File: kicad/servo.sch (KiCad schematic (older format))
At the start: 0 parts

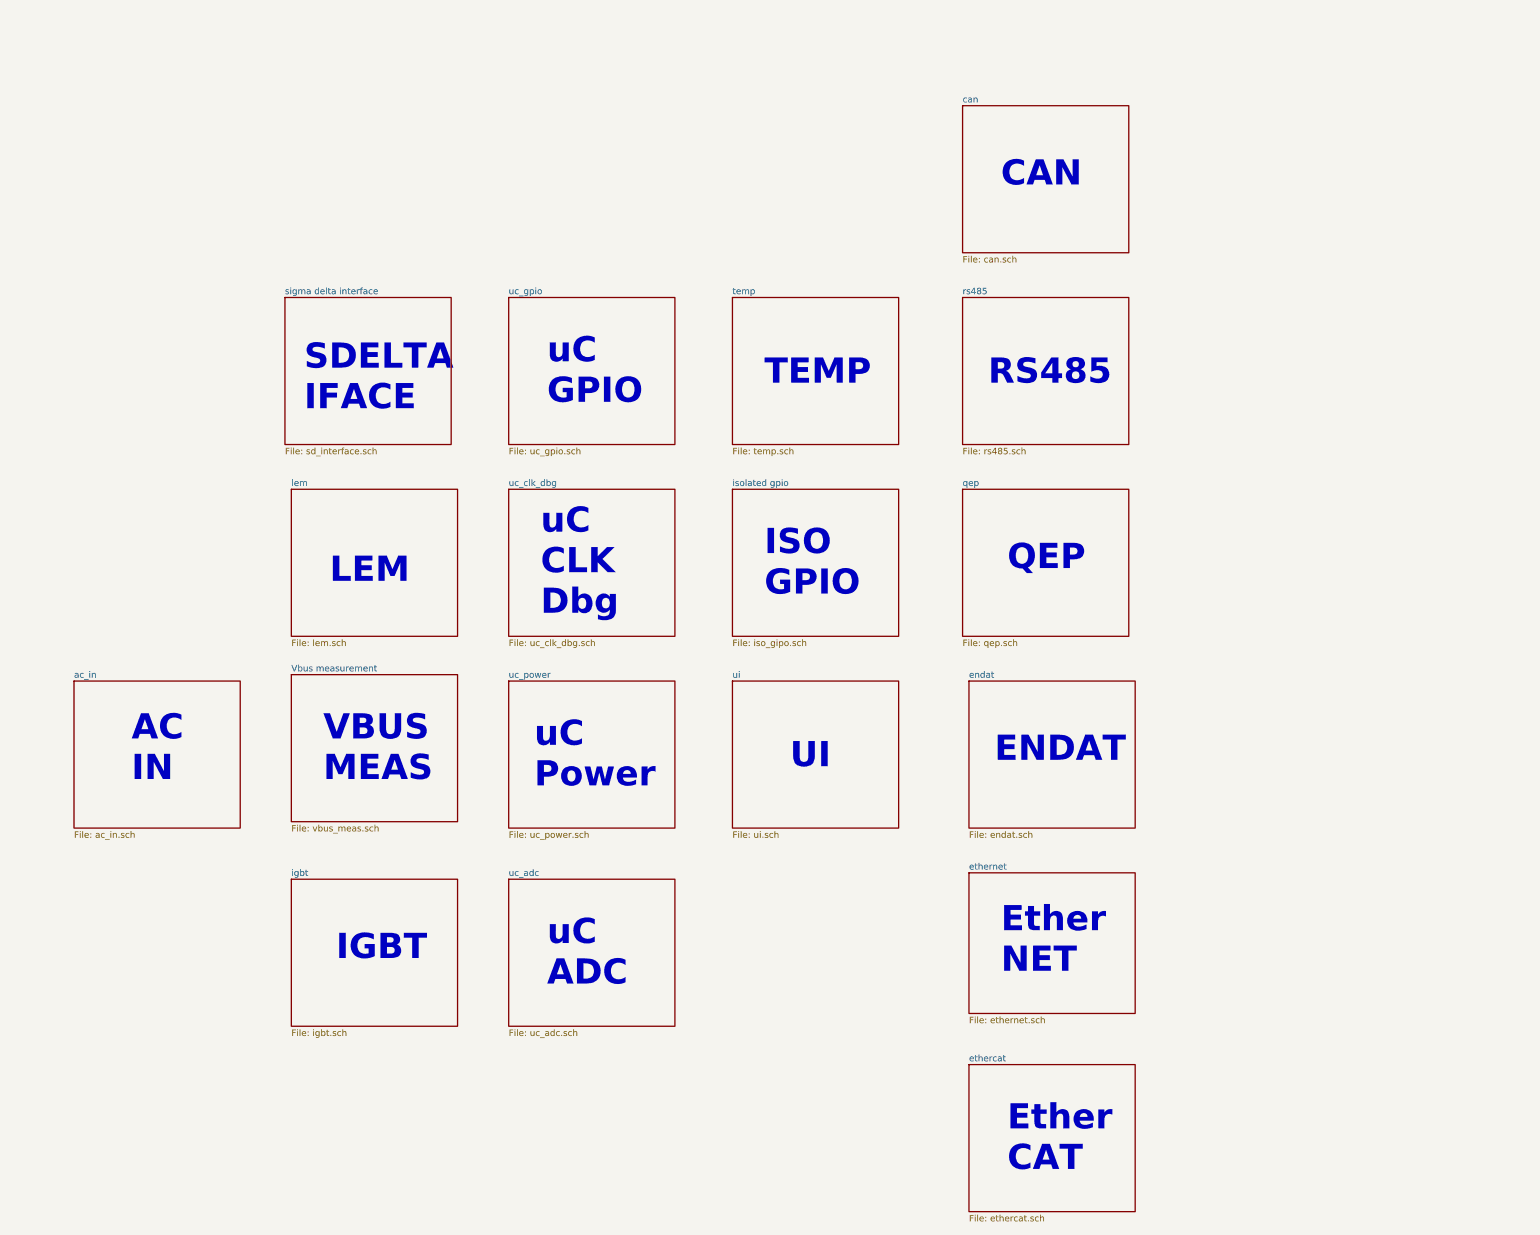
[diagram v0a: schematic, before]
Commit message: remove isolation GPIO's and replace it by free pins at IGBT
I remove completely the isolated inputs pins cause I've 8 pins free at
IGBT isolated interfase, so I leave 4 for outpus and 4 for inputs with
one isolated stage, the same as the previous isolated GPIO sheet..
I've improved the DBG sheet and some other details,. I'm ready to make
some electrical checks and fchoose the parts codes and footprints.. go
for it!
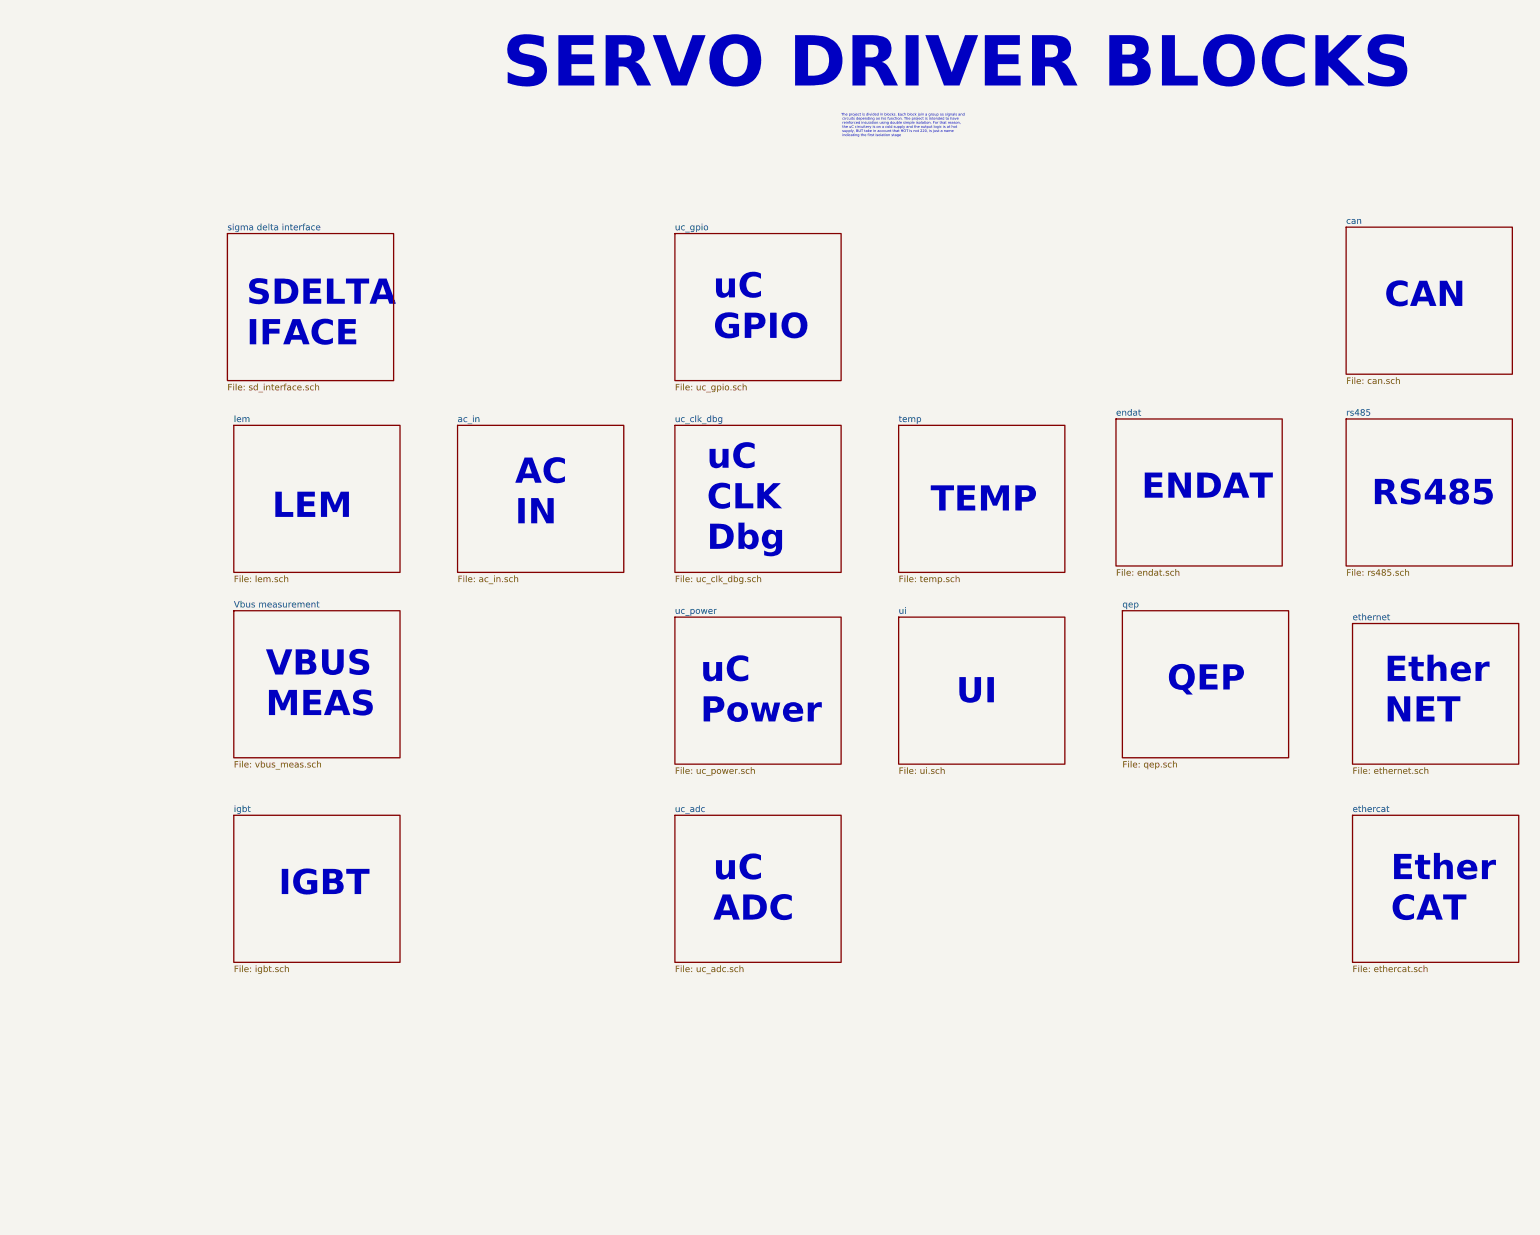
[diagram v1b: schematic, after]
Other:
- note added: "SERVO DRIVER BLOCKS"
- note added: "The project is divided in blocks. Each block join a group os signals and\n circuits depending on his function. The project is intended to have\n reinforced insulation using double simple isolation. For that reason,\n the uC circuitery is on a cold supply and the output logic is at hot\n supply, BUT take in account that HOT is not 220, is just a name\n indicating the first isolation stage\n"
- note removed: "ISO\nGPIO\n"
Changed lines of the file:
@@
 $Descr A3 16535 11693
 encoding utf-8
-Sheet 1 19
+Sheet 1 18
 Title "servo drive"
-Date "25 10 2019"
+Date "2020-01-09"
 Rev "1.0"
 Comp "dci"
@@
 $EndDescr
 $Sheet
-S 9350 7400 1300 1100
+S 12350 5450 1300 1100
 U 5DC3DC9E
 F0 "ethernet" 50
@@
 $EndSheet
 $Sheet
-S 5750 7450 1300 1150
+S 7050 6950 1300 1150
 U 5DD0E9D6
 F0 "uc_adc" 50
@@
 $EndSheet
 $Sheet
-S 9350 8900 1300 1150
+S 12350 6950 1300 1150
 U 5DC4A59D
 F0 "ethercat" 50
@@
 $EndSheet
 $Sheet
-S 5750 5900 1300 1150
+S 7050 5400 1300 1150
 U 5EAA846A
 F0 "uc_power" 50
@@
 $EndSheet
 $Sheet
-S 5750 4400 1300 1150
+S 7050 3900 1300 1150
 U 5DD4DF4C
 F0 "uc_clk_dbg" 50
@@
 $EndSheet
 $Sheet
-S 2350 5900 1300 1150
+S 5350 3900 1300 1150
 U 5DD76B18
 F0 "ac_in" 50
 F1 "ac_in.sch" 50
 $EndSheet
-Text Notes 6050 8300 0    197  ~ 39
+Text Notes 7350 7800 0    197  ~ 39
 uC\nADC
 $Sheet
-S 4050 7450 1300 1150
+S 3600 6950 1300 1150
 U 5DDE8C5E
 F0 "igbt" 50
 F1 "igbt.sch" 50
 $EndSheet
-Text Notes 4400 8100 0    197  ~ 39
+Text Notes 3950 7600 0    197  ~ 39
 IGBT
-Text Notes 5950 6750 0    197  ~ 39
+Text Notes 7250 6250 0    197  ~ 39
 uC \nPower
-Text Notes 9650 9750 0    197  ~ 39
+Text Notes 12650 7800 0    197  ~ 39
 Ether\nCAT
 $Sheet
-S 7500 2900 1300 1150
+S 8800 3900 1300 1150
 U 5DE49152
 F0 "temp" 50
 F1 "temp.sch" 50
 $EndSheet
-Text Notes 7750 3600 0    197  ~ 39
+Text Notes 9050 4600 0    197  ~ 39
 TEMP
-Text Notes 2800 6700 0    197  ~ 39
+Text Notes 5800 4700 0    197  ~ 39
 AC\nIN
-Text Notes 9600 8200 0    197  ~ 39
+Text Notes 12600 6250 0    197  ~ 39
 Ether\nNET
-Text Notes 6000 5400 0    197  ~ 39
+Text Notes 7300 4900 0    197  ~ 39
 uC\nCLK\nDbg
-Text Notes 9550 6550 0    197  ~ 39
+Text Notes 10700 4500 0    197  ~ 39
 ENDAT
 $Sheet
-S 9350 5900 1300 1150
+S 10500 3850 1300 1150
 U 5DE3DF56
 F0 "endat" 50
@@
 $EndSheet
 $Sheet
-S 9300 4400 1300 1150
+S 10550 5350 1300 1150
 U 5E092156
 F0 "qep" 50
 F1 "qep.sch" 50
 $EndSheet
-Text Notes 9650 5050 0    197  ~ 39
+Text Notes 10900 6000 0    197  ~ 39
 QEP
 $Sheet
-S 9300 2900 1300 1150
+S 12300 3850 1300 1150
 U 5E1BAEAA
 F0 "rs485" 50
 F1 "rs485.sch" 50
 $EndSheet
-Text Notes 9500 3600 0    197  ~ 39
+Text Notes 12500 4550 0    197  ~ 39
 RS485
 $Sheet
-S 9300 1400 1300 1150
+S 12300 2350 1300 1150
 U 5E21534F
 F0 "can" 50
 F1 "can.sch" 50
 $EndSheet
-Text Notes 9600 2050 0    197  ~ 39
+Text Notes 12600 3000 0    197  ~ 39
 CAN
 $Sheet
-S 5750 2900 1300 1150
+S 7050 2400 1300 1150
 U 5E033FE4
 F0 "uc_gpio" 50
 F1 "uc_gpio.sch" 50
 $EndSheet
-Text Notes 6050 3750 0    197  ~ 39
+Text Notes 7350 3250 0    197  ~ 39
 uC\nGPIO
 $Sheet
-S 7500 4400 1300 1150
-U 5E0D58C4
-F0 "isolated gpio" 50
-F1 "iso_gipo.sch" 50
-$EndSheet
-Text Notes 7750 5250 0    197  ~ 39
-ISO\nGPIO\n
-$Sheet
-S 7500 5900 1300 1150
+S 8800 5400 1300 1150
 U 5E72D841
 F0 "ui" 50
 F1 "ui.sch" 50
 $EndSheet
-Text Notes 7950 6600 0    197  ~ 39
+Text Notes 9250 6100 0    197  ~ 39
 UI
 $Sheet
-S 4050 4400 1300 1150
+S 3600 3900 1300 1150
 U 605B70F2
 F0 "lem" 50
 F1 "lem.sch" 50
 $EndSheet
-Text Notes 4350 5150 0    197  ~ 39
+Text Notes 3900 4650 0    197  ~ 39
 LEM
 $Sheet
-S 4050 5850 1300 1150
+S 3600 5350 1300 1150
 U 605BEC04
 F0 "Vbus measurement" 50
 F1 "vbus_meas.sch" 50
 $EndSheet
-Text Notes 4300 6700 0    197  ~ 39
+Text Notes 3850 6200 0    197  ~ 39
 VBUS\nMEAS
 $Sheet
-S 4000 2900 1300 1150
+S 3550 2400 1300 1150
 U 5EC40F3C
 F0 "sigma delta interface" 50
 F1 "sd_interface.sch" 50
 $EndSheet
-Text Notes 4150 3800 0    197  ~ 39
+Text Notes 3700 3300 0    197  ~ 39
 SDELTA\nIFACE
+Text Notes 5700 1300 0    394  ~ 79
+SERVO DRIVER BLOCKS
+Text Notes 8350 1650 0    20   ~ 0
+The project is divided in blocks. Each block join a group os signals and\n circuits depending on his function. The project is intended to have\n reinforced insulation using double simple isolation. For that reason,\n the uC circuitery is on a cold supply and the output logic is at hot\n supply, BUT take in account that HOT is not 220, is just a name\n indicating the first isolation stage\n
 $EndSCHEMATC

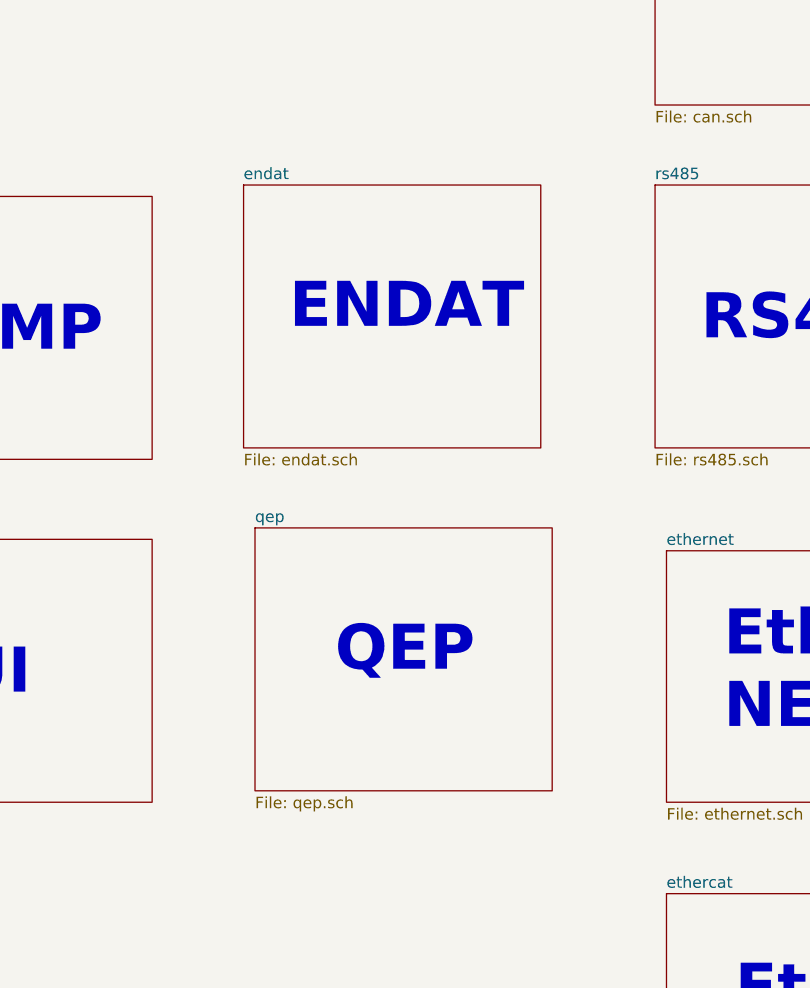
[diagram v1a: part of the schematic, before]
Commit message: added 4 push buttons and more gpios on LCD connector
just to have more UI options. With those I'd manage graphics LCD plus 4
buttons, and charaveter LCD. or the embedded EVE graphic LCD
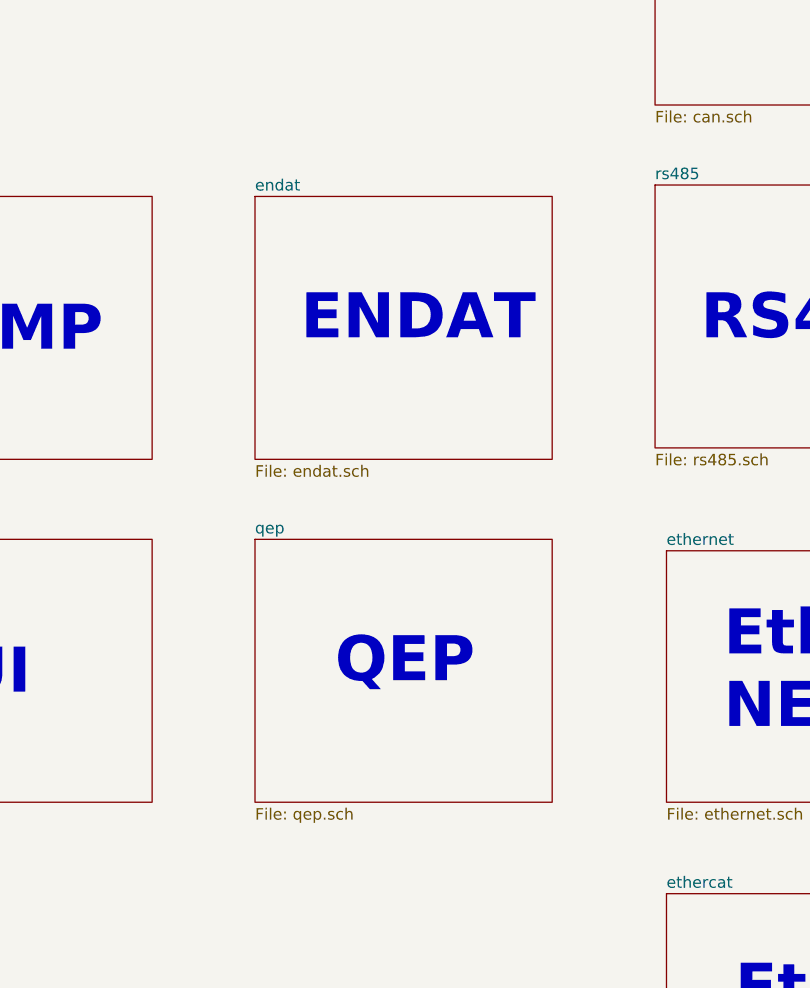
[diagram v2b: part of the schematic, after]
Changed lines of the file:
@@
 Text Notes 7300 4900 0    197  ~ 39
 uC\nCLK\nDbg
-Text Notes 10700 4500 0    197  ~ 39
+Text Notes 10750 4550 0    197  ~ 39
 ENDAT
 $Sheet
-S 10500 3850 1300 1150
+S 10550 3900 1300 1150
 U 5DE3DF56
 F0 "endat" 50
@@
 $EndSheet
 $Sheet
-S 10550 5350 1300 1150
+S 10550 5400 1300 1150
 U 5E092156
 F0 "qep" 50
 F1 "qep.sch" 50
 $EndSheet
-Text Notes 10900 6000 0    197  ~ 39
+Text Notes 10900 6050 0    197  ~ 39
 QEP
 $Sheet

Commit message: I've passed all footprin to layout BUT...
I've passed all, first glance... I need to confirm in details a lot of
things. The objetive for these is to have an aproximation of the size
I'll need to make the board.. then I choose the final detailed footprint
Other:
- note added: "CONN"
- note added: "SDELTA\n"
- note removed: "SDELTA\nIFACE"
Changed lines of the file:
@@
 $Descr A3 16535 11693
 encoding utf-8
-Sheet 1 18
+Sheet 1 19
 Title "servo drive"
 Date "2020-01-09"
@@
 S 3600 5350 1300 1150
 U 605BEC04
-F0 "Vbus measurement" 50
+F0 "Vbus meas" 50
 F1 "vbus_meas.sch" 50
 $EndSheet
@@
 VBUS\nMEAS
 $Sheet
-S 3550 2400 1300 1150
+S 8850 6950 1300 1150
 U 5EC40F3C
-F0 "sigma delta interface" 50
-F1 "sd_interface.sch" 50
+F0 "connectors" 50
+F1 "conn.sch" 50
 $EndSheet
-Text Notes 3700 3300 0    197  ~ 39
-SDELTA\nIFACE
+Text Notes 9100 7650 0    197  ~ 39
+CONN
 Text Notes 5700 1300 0    394  ~ 79
 SERVO DRIVER BLOCKS
 Text Notes 8350 1650 0    20   ~ 0
 The project is divided in blocks. Each block join a group os signals and\n circuits depending on his function. The project is intended to have\n reinforced insulation using double simple isolation. For that reason,\n the uC circuitery is on a cold supply and the output logic is at hot\n supply, BUT take in account that HOT is not 220, is just a name\n indicating the first isolation stage\n
+$Sheet
+S 3600 2350 1300 1150
+U 6056AA11
+F0 "sigma_delta" 50
+F1 "sigma_delta.sch" 50
+$EndSheet
+Text Notes 3700 3050 0    197  ~ 39
+SDELTA\n
 $EndSCHEMATC

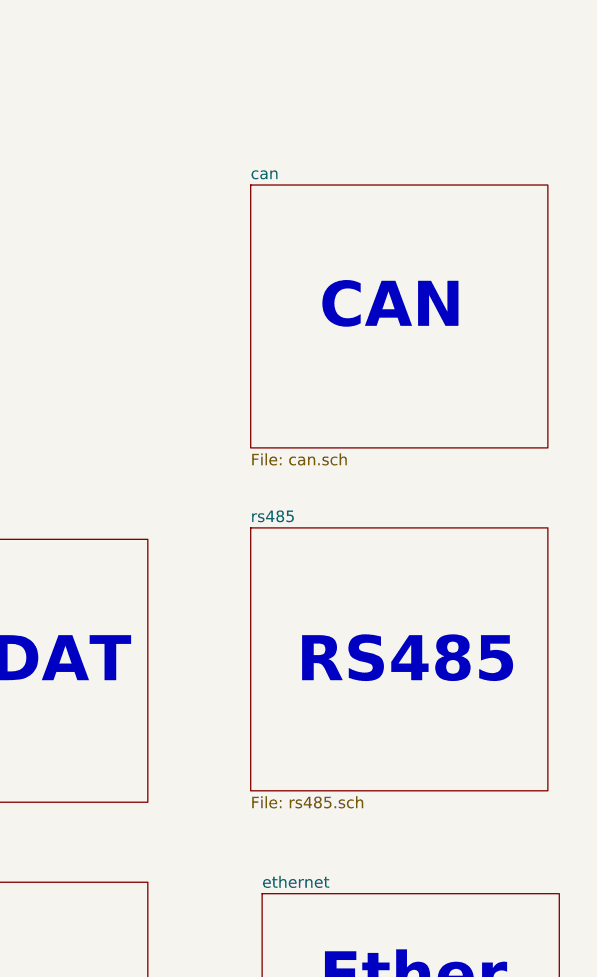
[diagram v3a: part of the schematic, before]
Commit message: changing single row terminal block to double row
I've changed to double row all the connectors, RJ45 and terminal blocks,
I saves spaces and also make it more intuitive related to user
interface..lets go
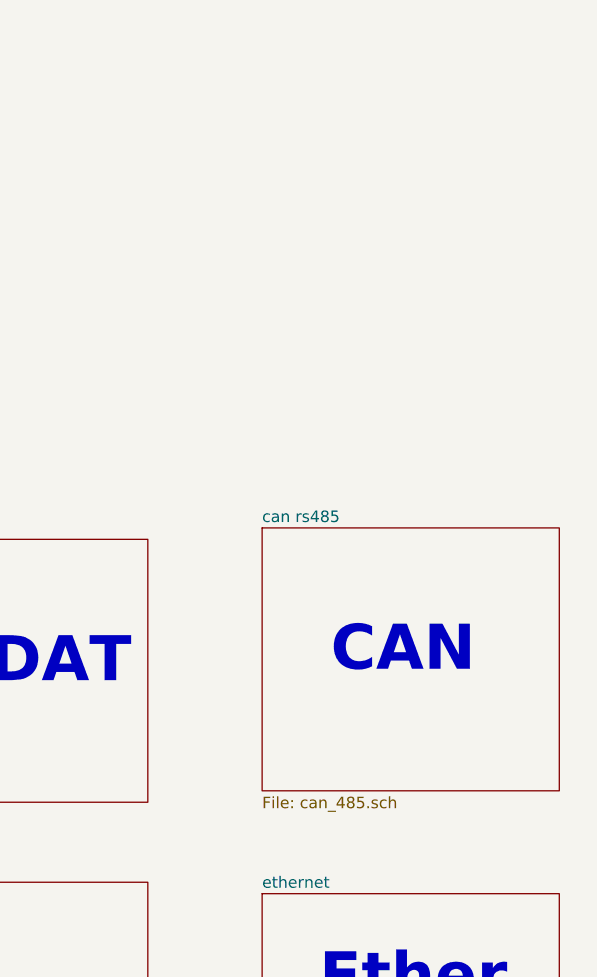
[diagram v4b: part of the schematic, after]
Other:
- note removed: "RS485"
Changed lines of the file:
@@
 $Descr A3 16535 11693
 encoding utf-8
-Sheet 1 19
+Sheet 1 18
 Title "servo drive"
 Date "2020-01-09"
@@
 QEP
 $Sheet
-S 12300 3850 1300 1150
-U 5E1BAEAA
-F0 "rs485" 50
-F1 "rs485.sch" 50
+S 12350 3850 1300 1150
+U 5E21534F
+F0 "can rs485" 50
+F1 "can_485.sch" 50
 $EndSheet
-Text Notes 12500 4550 0    197  ~ 39
-RS485
-$Sheet
-S 12300 2350 1300 1150
-U 5E21534F
-F0 "can" 50
-F1 "can.sch" 50
-$EndSheet
-Text Notes 12600 3000 0    197  ~ 39
+Text Notes 12650 4500 0    197  ~ 39
 CAN
 $Sheet
